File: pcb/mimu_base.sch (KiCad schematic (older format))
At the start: 16 parts, among them J1 OPT, SW2 SW_DPDT_x2, U1 AQY211EH, U2 ATTINY88AU

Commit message: Bump near-final version for battery powered version. Todo: Maybe remove the capacitor? Needs realworld-test.
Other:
- note added: "(4,5V-1,5V)/3mA = 1k\n( 3V-1,5V)/3mA = 500R"
- note added: "(4,5V-1.3V)/8mA = 400R\n( 3V-1.3V)/8mA = 333R"
- note removed: "(5,5V-1,5V)/3mA = 1,3k\n( 3V-1,5V)/3mA = 500R"
- note removed: "(5,5V-1.3V)/8mA = 500R\n( 3V-1.3V)/8mA = 333R"
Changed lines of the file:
@@
 	3400 5600 3300 5600
 Text Notes 2450 5600 2    50   ~ 0
-(5,5V-1.3V)/8mA = 500R\n(  3V-1.3V)/8mA = 333R
-Text Notes 2850 1850 0    50   ~ 0
-(5,5V-1,5V)/3mA = 1,3k\n(  3V-1,5V)/3mA = 500R
+(4,5V-1.3V)/8mA = 400R\n(  3V-1.3V)/8mA = 333R
+Text Notes 2850 2050 0    50   ~ 0
+(4,5V-1,5V)/3mA = 1k\n(  3V-1,5V)/3mA = 500R
 Text Notes 4000 2700 2    50   ~ 0
 I_Fon = 1.2mA-3mA

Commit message: Cap not needed for XLR
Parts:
- removed C3: 1uF, Capacitor_THT:C_Rect_L7.0mm_W3.5mm_P2.50mm_P5.00mm, symbol Device:C
- removed OUTPUT1: XLR3, Connector_PinHeader_2.54mm:PinHeader_1x03_P2.54mm_Vertical, symbol Connector:XLR3
- removed SW2: SW_DPDT_x2, Jumper:SolderJumper-3_P1.3mm_Bridged12_RoundedPad1.0x1.5mm, symbol Switch:SW_DPDT_x2
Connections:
- wire segments 79 -> 67
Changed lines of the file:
@@
 Wire Wire Line
 	4300 5150 4300 5300
-Wire Wire Line
-	4700 2800 4700 3050
-Wire Wire Line
-	4700 3050 4850 3050
-Wire Wire Line
-	5250 3200 5250 3150
-Wire Wire Line
-	5500 3200 5250 3200
-$Comp
-L Device:C C3
-U 1 1 5E6D3680
-P 5500 3050
-F 0 "C3" H 5600 3100 50  0000 L CNN
-F 1 "1uF" H 5350 2800 50  0000 L CNN
-F 2 "Capacitor_THT:C_Rect_L7.0mm_W3.5mm_P2.50mm_P5.00mm" H 5538 2900 50  0001 C CNN
-F 3 "~" H 5500 3050 50  0001 C CNN
-	1    5500 3050
-	1    0    0    -1
-$EndComp
-Connection ~ 5500 2900
-Wire Wire Line
-	5250 2900 5500 2900
-Wire Wire Line
-	5250 2950 5250 2900
-Wire Wire Line
-	4700 2800 4550 2800
-$Comp
-L Switch:SW_DPDT_x2 SW2
-U 1 1 5E6D3676
-P 5050 3050
-F 0 "SW2" H 5050 3335 50  0000 C CNN
-F 1 "SW_DPDT_x2" H 5050 3244 50  0000 C CNN
-F 2 "Jumper:SolderJumper-3_P1.3mm_Bridged12_RoundedPad1.0x1.5mm" H 5050 3050 50  0001 C CNN
-F 3 "~" H 5050 3050 50  0001 C CNN
-	1    5050 3050
-	1    0    0    -1
-$EndComp
 $Comp
 L power:GND #PWR014
@@
 	1    0    0    -1
 $EndComp
-Connection ~ 5150 2550
 Wire Wire Line
 	4550 2600 5150 2600
@@
 	5150 2600 5150 2550
 Wire Wire Line
-	5650 2550 5650 1850
-Wire Wire Line
-	5150 2550 5650 2550
-Wire Wire Line
-	5500 2250 5500 2900
-Connection ~ 5500 2250
-Wire Wire Line
-	5450 2250 5500 2250
-Wire Wire Line
-	4850 2250 4800 2250
+	5150 2550 5150 1850
 Wire Wire Line
 	5500 1450 5500 1700
 Wire Wire Line
 	4800 1450 4800 1850
-Wire Wire Line
-	5150 1850 5650 1850
-$Comp
-L Connector:XLR3 OUTPUT1
-U 1 1 5E6D3630
-P 5150 2250
-F 0 "OUTPUT1" H 5150 2500 50  0000 C CNN
-F 1 "XLR3" H 5350 2000 50  0000 C CNN
-F 2 "Connector_PinHeader_2.54mm:PinHeader_1x03_P2.54mm_Vertical" H 5150 2250 50  0001 C CNN
-F 3 "" H 5150 2250 50  0001 C CNN
-	1    5150 2250
-	1    0    0    -1
-$EndComp
 Wire Wire Line
 	3950 3050 3950 2800
@@
 Wire Wire Line
 	4550 1850 4800 1850
-Connection ~ 4800 1850
-Wire Wire Line
-	4800 1850 4800 2250
 Wire Wire Line
 	6000 1600 6000 1700
@@
 Connection ~ 5500 1700
 Wire Wire Line
-	5500 1700 5500 2250
-Wire Wire Line
 	6200 1600 6200 1850
 Wire Wire Line
-	6200 1850 5650 1850
-Connection ~ 5650 1850
+	6200 1850 5150 1850
+Connection ~ 5150 1850
 $Comp
 L Connector:TestPoint TP5
@@
 Text Notes 4000 2700 2    50   ~ 0
 I_Fon = 1.2mA-3mA
+Wire Wire Line
+	4550 2800 5500 2800
+Wire Wire Line
+	5500 1700 5500 2800
 $EndSCHEMATC

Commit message: This might actually work
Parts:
- removed D_LED1: LED, LED_THT:LED_D3.0mm, symbol Device:LED
- removed RV1: 1K_POT, Potentiometer_THT:Potentiometer_Bourns_PTV09A-2_Single_Horizontal, symbol Device:R_POT
- removed TP5: TestPoint, Measurement_Points:Measurement_Point_Round-SMD-Pad_Small, symbol Connector:TestPoint
- added D2: LED_Dual_ACA, LED_THT:LED_Rectangular_W5.0mm_H2.0mm-3Pins, symbol Device:LED_Dual_ACA
- added R5: 390R, Capacitor_SMD:C_1206_3216Metric_Pad1.33x1.80mm_HandSolder, symbol Device:R
- added R6: 100R, Capacitor_SMD:C_1206_3216Metric_Pad1.33x1.80mm_HandSolder, symbol mimu_phantom-rescue:R-mimu3000-rescue-mimu_phantom-rescue
- added R7: 1k, Capacitor_SMD:C_1206_3216Metric_Pad1.33x1.80mm_HandSolder, symbol mimu_phantom-rescue:R-mimu3000-rescue-mimu_phantom-rescue
- added SW1: SW_Push, digikey:Switch_Tactile_SMD_6x6mm_PTS645, symbol Switch:SW_MEC_5E
- added U4: H11F1M, Package_DIP:DIP-6_W7.62mm, symbol mimu_phantom-rescue:H11F1M
- R1: value 333R -> 390R; footprint Resistor_SMD:R_1206_3216Metric_Pad1.42x1.75mm_HandSolder -> Capacitor_SMD:C_1206_3216Metric_Pad1.33x1.80mm_HandSolder
- R2: symbol mimu_phantom-rescue:R-mimu3000-rescue -> mimu_phantom-rescue:R-mimu3000-rescue-mimu_phantom-rescue
- SENS1: symbol custom:Conn_TOF_flipped -> mimu_phantom-rescue:Conn_TOF_flipped-custom
- U1: symbol custom:H11F1M -> mimu_phantom-rescue:H11F1M-custom
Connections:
- net +3V0 is gone; now on net VCC: ISP1.2 (VCC)
- net GND: now also D2.2 (K), SW1.3 (K), U4.2
- net VCC: now also R7.2
- net XLR_COLD: now also U4.6
- net XLR_HOT: now also U4.4
- net at R1.2: now also D2.1 (A1)
- net BUTT: now reaches U2.20 (PC7)
- net BUTT: now also R7.1, SW1.2
- net LED_G: now reaches U2.26 (PC3)
- net LED_G: now also R5.1
- net LED renamed LED_R
- net POT renamed ATT
- net ATT: now also R6.1
- new net: D2.3 (A2), R5.2
- new net: R6.2, U4.1
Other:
- note added: "(4,5V-1,5V)/30mA = 100R\n( 3V-1,5V)/30mA = 50R"
- moved on the sheet: INPUT1, R2, SENS1, U1

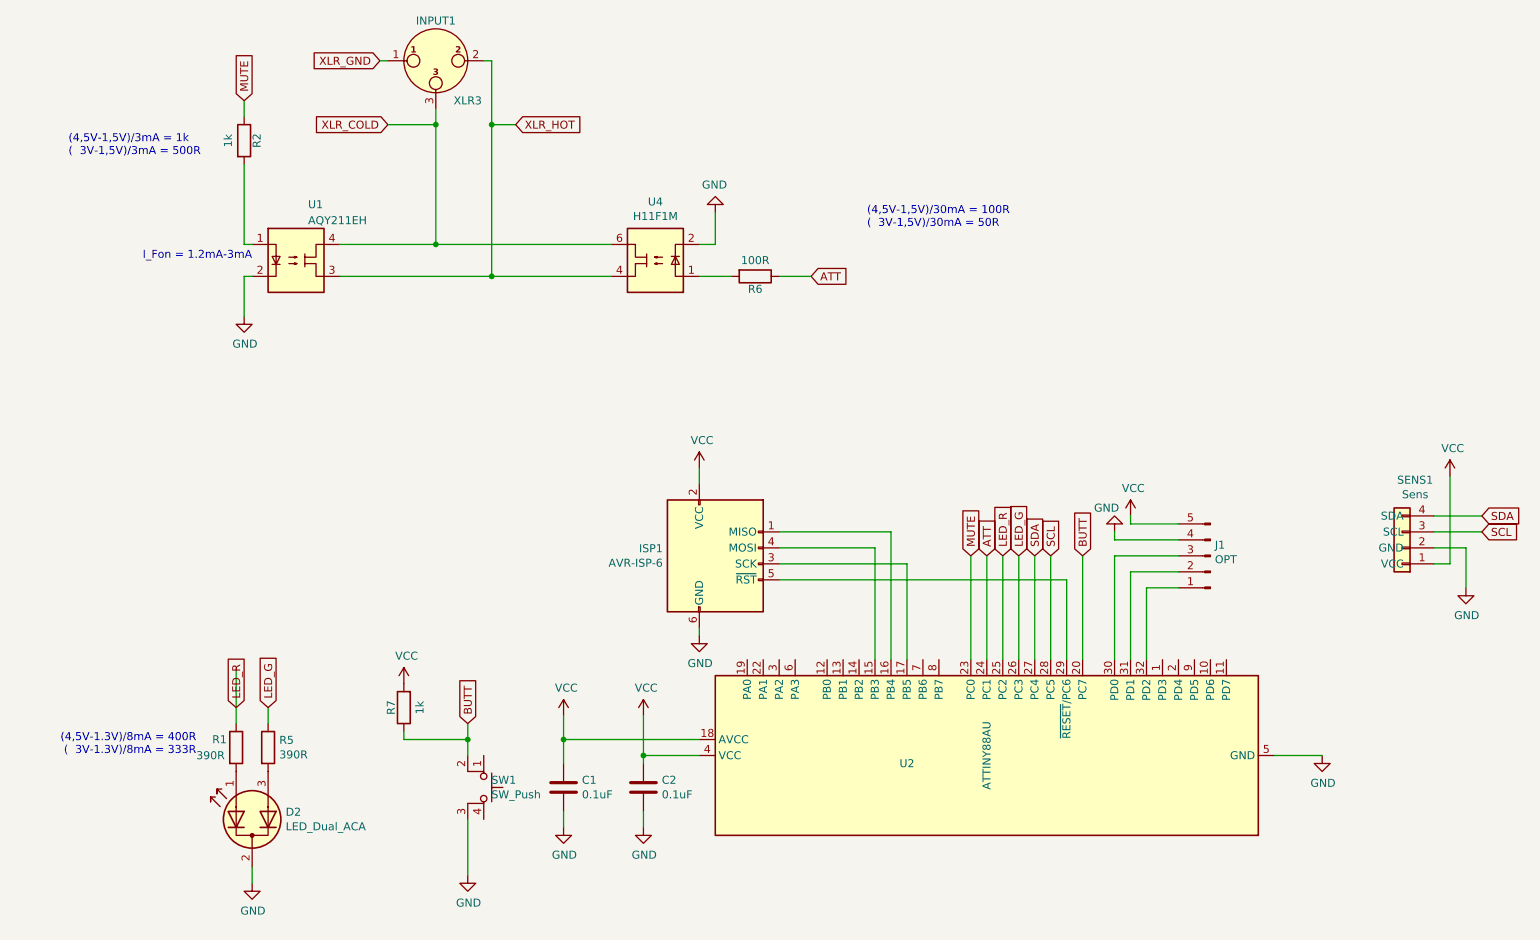
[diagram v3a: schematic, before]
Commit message: Connected Attenuation to PWM-Able pin
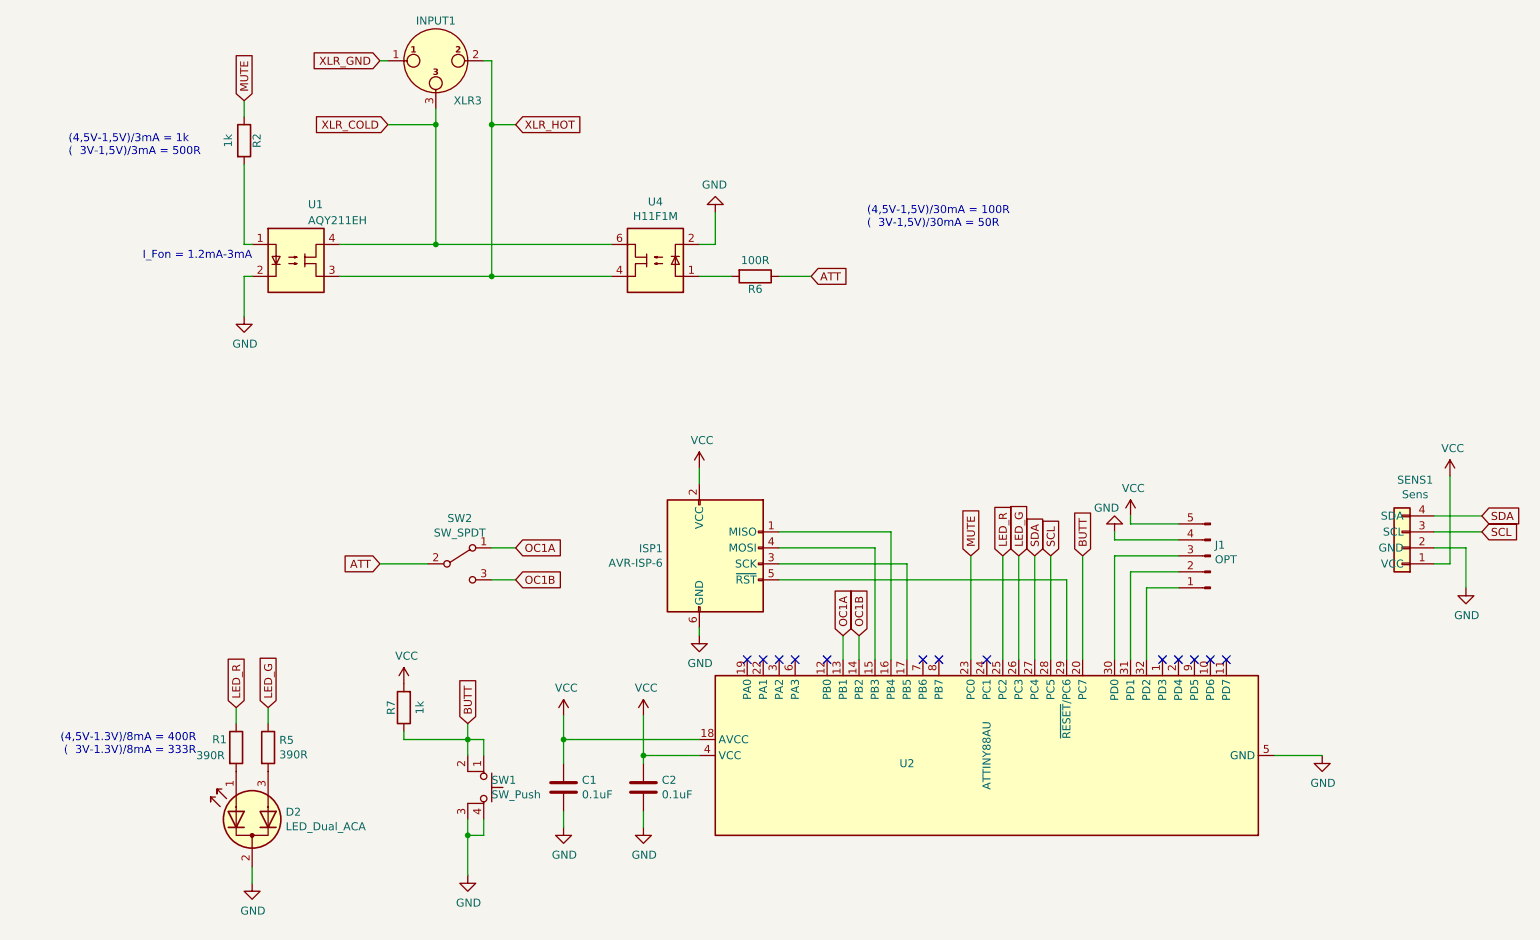
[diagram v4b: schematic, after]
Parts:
- added SW2: SW_SPDT, Jumper:SolderJumper-3_P1.3mm_Bridged12_RoundedPad1.0x1.5mm_NumberLabels, symbol Switch:SW_SPDT
- SENS1: footprint Connector_PinHeader_2.54mm:PinHeader_1x04_P2.54mm_Horizontal -> Connector_PinHeader_2.54mm:PinHeader_1x04_P2.54mm_Vertical
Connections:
- net ATT: now also SW2.2 (B); no longer U2.24 (PC1)
- net BUTT: now also SW1.1
- net GND: now also SW1.4 (A)
- net OC1A: now reaches U2.13 (PB1)
- net OC1A: now also SW2.1 (A)
- net OC1B: now reaches U2.14 (PB2)
- net OC1B: now also SW2.3 (C)
- no-connect marks 0 -> 13
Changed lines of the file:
@@
 Text GLabel 2300 1300 1    50   Input ~ 0
 MUTE
-Wire Wire Line
-	6950 4800 6950 4150
 Text GLabel 7550 4150 1    50   Input ~ 0
 BUTT
@@
 Text GLabel 2250 5100 1    50   Input ~ 0
 LED_R
-Wire Wire Line
-	2250 4850 2250 5200
 $Comp
 L power:GND #PWR05
@@
 F 0 "SENS1" H 9468 3675 50  0000 C CNN
 F 1 "Sens" H 9468 3766 50  0000 C CNN
-F 2 "Connector_PinHeader_2.54mm:PinHeader_1x04_P2.54mm_Horizontal" H 9550 4100 50  0001 C CNN
+F 2 "Connector_PinHeader_2.54mm:PinHeader_1x04_P2.54mm_Vertical" H 9550 4100 50  0001 C CNN
 F 3 "~" H 9550 4100 50  0001 C CNN
 	1    9550 4100
@@
 	2450 5200 2450 5100
 Wire Wire Line
-	3700 5800 3700 6150
+	3700 5800 3700 5900
 Text GLabel 7150 4150 1    50   Input ~ 0
 LED_G
 Wire Wire Line
 	7150 4800 7150 4150
-Text GLabel 6950 4150 1    50   Input ~ 0
+Text GLabel 3150 4200 0    50   Input ~ 0
 ATT
 Wire Wire Line
@@
 	1    0    0    -1
 $EndComp
+$Comp
+L Switch:SW_SPDT SW2
+U 1 1 616EBE4E
+P 3650 4200
+F 0 "SW2" H 3650 4485 50  0000 C CNN
+F 1 "SW_SPDT" H 3650 4394 50  0000 C CNN
+F 2 "Jumper:SolderJumper-3_P1.3mm_Bridged12_RoundedPad1.0x1.5mm_NumberLabels" H 3650 4200 50  0001 C CNN
+F 3 "~" H 3650 4200 50  0001 C CNN
+	1    3650 4200
+	1    0    0    -1
+$EndComp
+Wire Wire Line
+	3150 4200 3450 4200
+Text GLabel 6050 4650 1    50   Input ~ 0
+OC1A
+Text GLabel 6150 4650 1    50   Input ~ 0
+OC1B
+Text GLabel 4000 4100 2    50   Input ~ 0
+OC1A
+Text GLabel 4000 4300 2    50   Input ~ 0
+OC1B
+Wire Wire Line
+	3850 4100 4000 4100
+Wire Wire Line
+	4000 4300 3850 4300
+Wire Wire Line
+	6150 4800 6150 4650
+Wire Wire Line
+	6050 4650 6050 4800
+NoConn ~ 8450 4800
+NoConn ~ 8350 4800
+NoConn ~ 8250 4800
+NoConn ~ 8150 4800
+NoConn ~ 8050 4800
+NoConn ~ 6950 4800
+NoConn ~ 6550 4800
+NoConn ~ 6650 4800
+NoConn ~ 5950 4800
+NoConn ~ 5750 4800
+NoConn ~ 5650 4800
+NoConn ~ 5550 4800
+NoConn ~ 5450 4800
+Wire Wire Line
+	3700 5300 3800 5300
+Wire Wire Line
+	3800 5300 3800 5400
+Wire Wire Line
+	3800 5800 3800 5900
+Wire Wire Line
+	3800 5900 3700 5900
+Connection ~ 3700 5900
+Wire Wire Line
+	3700 5900 3700 6150
+Wire Wire Line
+	2250 5100 2250 5200
 $EndSCHEMATC
